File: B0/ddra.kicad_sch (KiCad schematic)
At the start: 5 parts, among them U003 74HCT244, U007 74HCT32, U023 74HCT377, U028 74HCT00, U029 74HCT00

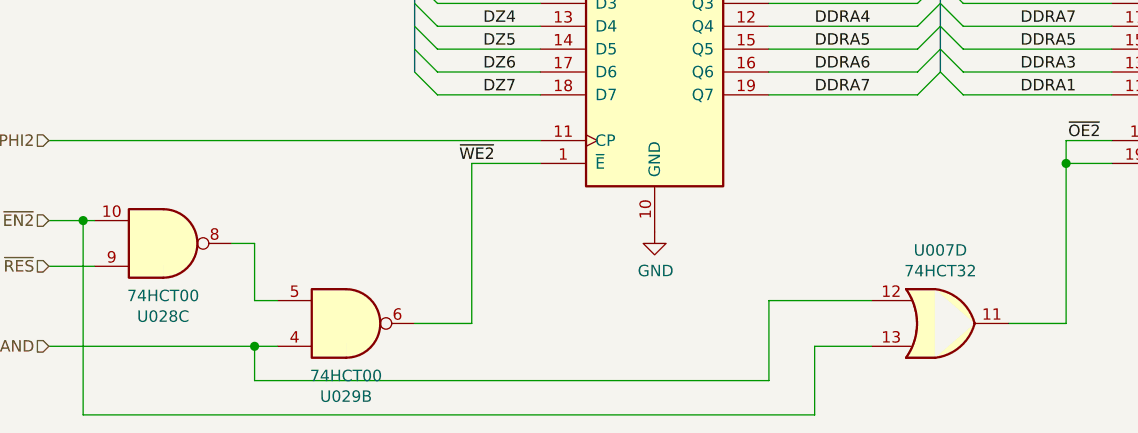
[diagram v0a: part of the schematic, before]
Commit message: B1 CREGA added
Work started on b1. CREGA added.
Minor changes to B0 schematic properties.
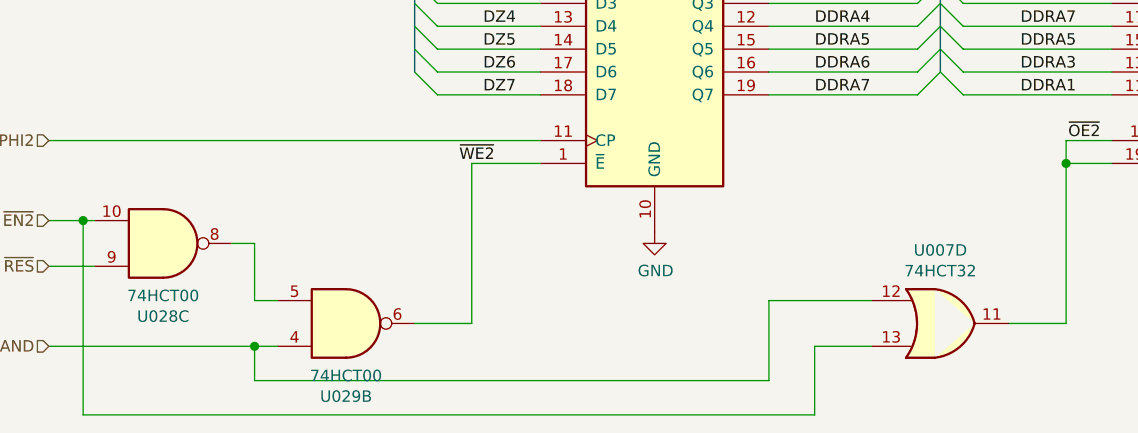
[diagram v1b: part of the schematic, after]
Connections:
- net ~EN2 renamed ~{EN2}
- net ~OE2 renamed ~{OE2}
- net ~RES renamed ~{RES}
- net ~WE2 renamed ~{WE2}

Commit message: .
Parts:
- U003: value 74HCT244 -> 74HC244
- U007: value 74HCT32 -> 74HC32
- U023: value 74HCT377 -> 74HC377
- U028, U029: value 74HCT00 -> 74HC00
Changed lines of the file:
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@@
     (in_bom yes) (on_board yes)
     (property "Reference" "U007" (id 0) (at 173.99 84.5882 0))
-    (property "Value" "74HCT32" (id 1) (at 173.99 86.8869 0))
+    (property "Value" "74HC32" (id 1) (at 173.99 86.8869 0))
     (property "Footprint" "74hct6526.footprints:SO-14" (id 2) (at 173.99 92.71 0)
       (effects (font (size 1.27 1.27)) hide)
@@
     (in_bom yes) (on_board yes)
     (property "Reference" "U003" (id 0) (at 213.36 41.2558 0))
-    (property "Value" "74HCT244" (id 1) (at 213.36 43.5545 0))
+    (property "Value" "74HC244" (id 1) (at 213.36 43.5545 0))
     (property "Footprint" "74hct6526.footprints:SOIC-20W" (id 2) (at 205.74 62.23 0)
       (effects (font (size 1.27 1.27)) hide)
@@
     (in_bom yes) (on_board yes)
     (property "Reference" "U029" (id 0) (at 107.95 100.8318 0))
-    (property "Value" "74HCT00" (id 1) (at 107.95 98.5331 0))
+    (property "Value" "74HC00" (id 1) (at 107.95 98.5331 0))
     (property "Footprint" "74hct6526.footprints:SO-14" (id 2) (at 107.95 92.71 0)
       (effects (font (size 1.27 1.27)) hide)
@@
     (in_bom yes) (on_board yes)
     (property "Reference" "U023" (id 0) (at 148.59 41.2558 0))
-    (property "Value" "74HCT377" (id 1) (at 148.59 43.5545 0))
+    (property "Value" "74HC377" (id 1) (at 148.59 43.5545 0))
     (property "Footprint" "74hct6526.footprints:SOIC-20W" (id 2) (at 142.24 62.23 0)
       (effects (font (size 1.27 1.27)) hide)
@@
     (in_bom yes) (on_board yes)
     (property "Reference" "U028" (id 0) (at 87.63 91.9418 0))
-    (property "Value" "74HCT00" (id 1) (at 87.63 89.6431 0))
+    (property "Value" "74HC00" (id 1) (at 87.63 89.6431 0))
     (property "Footprint" "74hct6526.footprints:SO-14" (id 2) (at 87.63 83.82 0)
       (effects (font (size 1.27 1.27)) hide)
